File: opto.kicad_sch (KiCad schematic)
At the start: 3 parts, among them U1 PC817

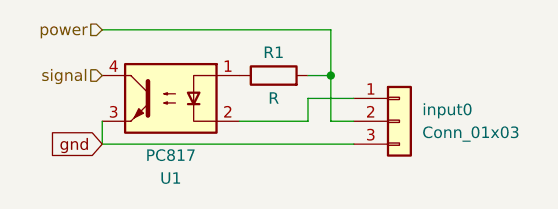
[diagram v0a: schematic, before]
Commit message: fixing labels / add some values
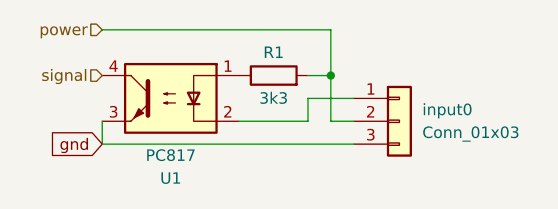
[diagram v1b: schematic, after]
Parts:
- R1: value R -> 3k3
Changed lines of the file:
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@@
       (effects (font (size 1.27 1.27)))
     )
-    (property "Value" "R" (at 90.17 58.42 90)
+    (property "Value" "3k3" (at 90.17 58.42 90)
       (effects (font (size 1.27 1.27)))
     )
